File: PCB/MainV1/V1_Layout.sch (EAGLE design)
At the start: 22 parts, among them IC3 AD623R, U2 MB85RC256VPF-G-JNERE2

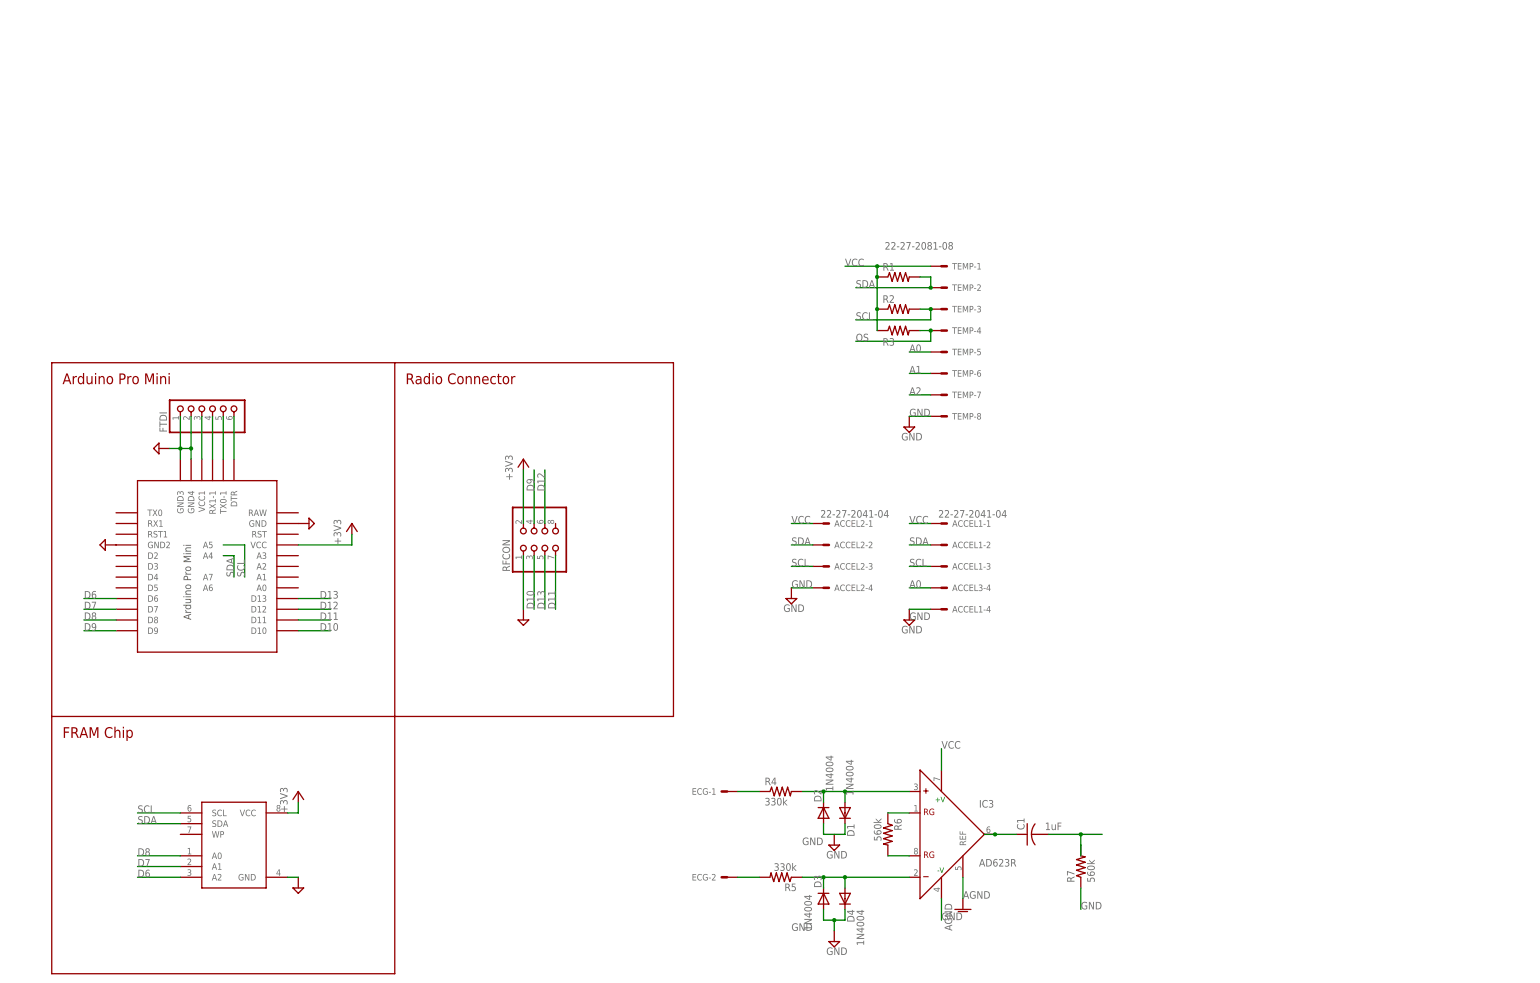
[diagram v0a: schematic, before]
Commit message: working on schematic, and first commit of temperature buddy board
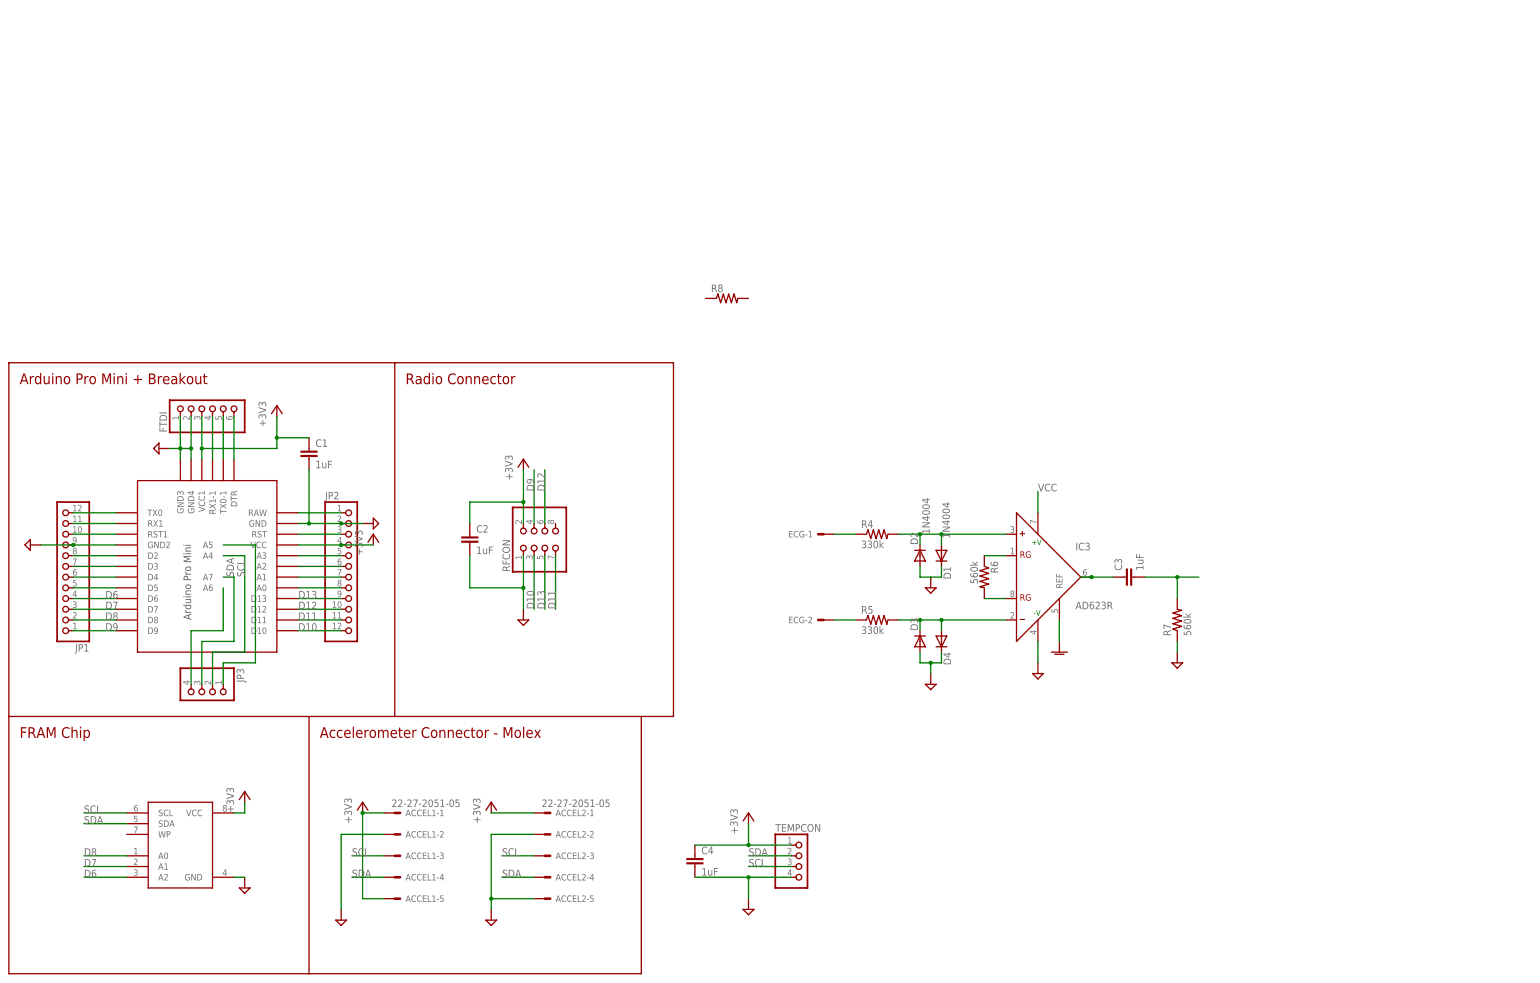
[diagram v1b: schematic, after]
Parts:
- removed ACCEL3: 22-27-2041-04, con-molex:22-27-2041-04
- removed R1, R2, R3: (no value), rcl:R-US_R0805
- removed TEMP: 22-27-2081-08, con-molex:22-27-2081-08
- added C2, C3, C4: 1uF, rcl:C-EUC0603
- added JP1, JP2: (no value), pinhead:PINHD-1X12
- added JP3: (no value), pinhead:PINHD-1X4
- added R8: (no value), rcl:R-US_R0603
- added TEMPCON: (no value), pinhead2:PINHD-1X4M
- ACCEL1, ACCEL2: value 22-27-2041-04 -> 22-27-2051-05; device con-molex:22-27-2041-04 -> con-molex:22-27-2051-05
- C1: device rcl:C-USC0805 -> rcl:C-EUC0603
- R4, R5, R7: device rcl:R-US_R0805 -> rcl:R-US_R0603
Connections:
- removed net A0: ACCEL3-4.S, TEMP-5.S
- removed net A1: TEMP-6.S
- removed net A2: TEMP-7.S
- removed net N$15: FTDI.3, U$1.VCC1
- removed net OS: R3.2, TEMP-4.S
- new net N$10: JP1.11, U$1.RX1
- new net N$11: JP1.10, U$1.RST1
- new net N$17: JP1.8, U$1.D2
- new net N$18: JP1.7, U$1.D3
- new net N$19: JP1.6, U$1.D4
- new net N$20: JP1.5, U$1.D5
- new net N$21: JP2.1, U$1.RAW
- new net N$23: JP2.3, U$1.RST
- new net N$24: JP2.5, U$1.A3
- new net N$25: JP2.6, U$1.A2
- new net N$26: JP2.7, U$1.A1
- new net N$27: JP2.8, U$1.A0
- new net N$28: JP3.4, U$1.A6
- new net N$29: JP3.3, U$1.A7
- new net N$9: JP1.12, U$1.TX0
- net +3V3: now also ACCEL1-1.S, ACCEL1-5.S, ACCEL2-1.S, C1.1, C2.1, C4.1, FTDI.3, JP2.4, TEMPCON.1, U$1.VCC1
- net D10: now also JP2.12
- net D11: now also JP2.11
- net D12: now also JP2.10
- net D13: now also JP2.9
- net D6: now also JP1.4
- net D7: now also JP1.3
- net D8: now also JP1.2
- net D9: now also JP1.1
- net GND: now also ACCEL1-2.S, ACCEL2-2.S, ACCEL2-5.S, C2.2, C3.2, C4.2, JP1.9, JP2.2, TEMPCON.4; no longer ACCEL1-4.S, ACCEL2-4.S, TEMP-8.S
- net N$2: now also R5.2; no longer R5.1
- net N$4: now also R5.1; no longer R5.2
- net N$6: now also C3.1; no longer C1.1
- net SCL: now also JP3.1, TEMPCON.3; no longer R2.2, TEMP-3.S
- net SDA: now also ACCEL1-4.S, ACCEL2-4.S, JP3.2, TEMPCON.2; no longer ACCEL1-2.S, ACCEL2-2.S, R1.2, TEMP-2.S
- net VCC: no longer ACCEL1-1.S, ACCEL2-1.S, R1.1, R2.1, R3.1, TEMP-1.S
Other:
- note added: "Accelerometer Connector - Molex"
- note added: "Arduino Pro Mini + Breakout"
- note removed: "Arduino Pro Mini"
- moved on the sheet: ACCEL1-1, ACCEL1-2, ACCEL1-3, ACCEL1-4, ACCEL2-1, ACCEL2-2, ACCEL2-3, ACCEL2-4, C1, D1, D2, D3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

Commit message: Changes ready for digital schematic design review (ECG STILL TODO)
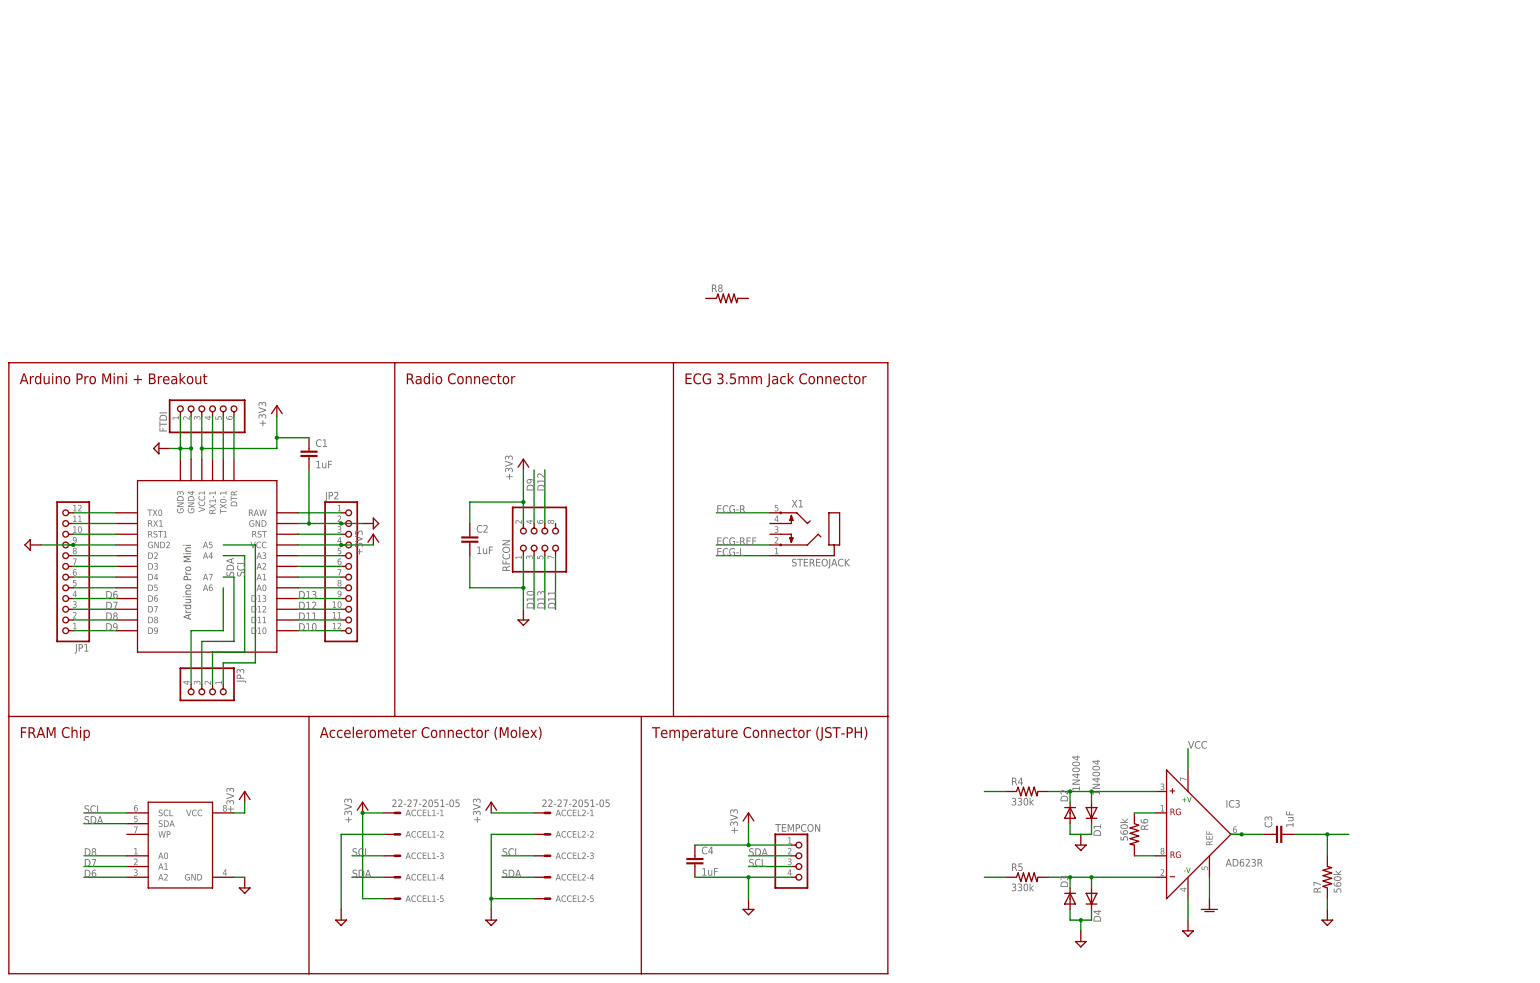
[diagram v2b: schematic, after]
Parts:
- removed ECG: 22-27-2021-02, con-molex:22-27-2021-02
- added X1: STEREOJACK, adafruit:STEREOJACK
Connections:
- new net ECG-L: X1.1
- new net ECG-R: X1.5
- new net ECG-REF: X1.2
- net N$1: no longer ECG-1.S
- net N$4: no longer ECG-2.S
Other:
- note added: "Accelerometer Connector (Molex)"
- note added: "ECG 3.5mm Jack Connector"
- note added: "Temperature Connector (JST-PH)"
- note removed: "Accelerometer Connector - Molex"
- moved on the sheet: C3, D1, D2, D3, D4, IC3, R4, R5, R6, R7

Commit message: main schematic ready for review
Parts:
- added D5, D6: (no value), diode:SCHOTTKY-DIODEDO35-7
- added D7, D8: 1N4004, diode:1N4004
- added IC1: AD826N, analog-devices:AD826N
- added PWR: (no value), pinhead:PINHD-1X2
- added R1, R2: 100k, rcl:R-US_R0603
- added R3: 330k, rcl:R-US_R0603
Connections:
- removed net N$1: R4.1
- removed net N$27: JP2.8, U$1.A0
- removed net N$4 (its old number): R5.1
- removed net VCC: IC3.+V
- new net A0: C3.2, D5.C, D6.A, JP2.8, R7.2, U$1.A0
- new net N$3: IC1A.IN+, R1.1, R2.2
- net +3V3: now also D6.C, IC1P.V+, IC3.+V, R1.2
- net AGND: now also D7.C, D8.A, IC1A.IN-, IC1A.OUT, R3.2
- net ECG-L: now also R4.1
- net ECG-R: now also R5.1
- net ECG-REF: now also R3.1
- net GND: now also D5.A, D7.A, D8.C, IC1B.IN+, IC1B.IN-, IC1P.V-, PWR.1, R2.1; no longer C3.2, R7.2
- net N$21: now also PWR.2
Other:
- note added: "EGC Signal Aplification"
- note added: "Pseudo-Ground"
- moved on the sheet: C3, D1, D2, D3, D4, FTDI, IC3, R4, R5, R6, R7

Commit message: Schematic cleanup, added bypass caps, added inndicator LEDs
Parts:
- added C10: (no value), rcl:CPOL-EUE3.5-8
- added C11, C8, C9: (no value), rcl:C-EU025-030X050
- added C5, C7: 1uF, rcl:C-EUC0603
- added C6: 100nF, rcl:C-EUC0603
- added IND1, IND2, IND3, PWR1: (no value), led:LEDCHIPLED_0805
- added R10, R9: 10k, rcl:R-US_R0603
- added R11, R12, R13: 150R, rcl:R-US_R0603
- R8: value (none) -> 150R
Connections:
- removed net N$18: JP1.7, U$1.D3
- removed net N$19: JP1.6, U$1.D4
- removed net N$20: JP1.5, U$1.D5
- new net D3: IND1.A, JP1.7, U$1.D3
- new net D4: IND2.A, JP1.6, U$1.D4
- new net D5: IND3.A, JP1.5, U$1.D5
- new net N$1: PWR1.C, R11.2
- new net N$14: IND1.C, R8.2
- new net N$15: IND2.C, R12.2
- new net N$16: IND3.C, R13.2
- net +3V3: now also C10.+, C11.1, C5.2, C6.1, C7.1, C8.1, C9.1, PWR1.A, R10.2, R9.2
- net GND: now also C10.-, C11.2, C5.1, C6.2, C7.2, C8.2, C9.2, R11.1, R12.1, R13.1, R8.1
- net SCL: now also R9.1
- net SDA: now also R10.1
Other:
- note added: "Address changable from Arduino"
- note added: "Extra Bypass Capacitors"
- note added: "Power + Indicator LEDs"
- moved on the sheet: ACCEL1-1, ACCEL1-2, ACCEL1-3, ACCEL1-4, ACCEL1-5, ACCEL2-1, ACCEL2-2, ACCEL2-3, ACCEL2-4, ACCEL2-5, C1, C2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
